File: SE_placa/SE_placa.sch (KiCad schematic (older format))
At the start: 53 parts, among them J1 5V, J2 Micro_SD_Card_Det_Hirose_DM3AT, J3 Conn_02x07_ESP32_IO, J4 I2C-0, J5 I2C-1, J6 Conn_02x03_LORA_IO, J7 U.FL-R-SMT(01), J8 UART, J9 Connector Bateria, Q1 BSS138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

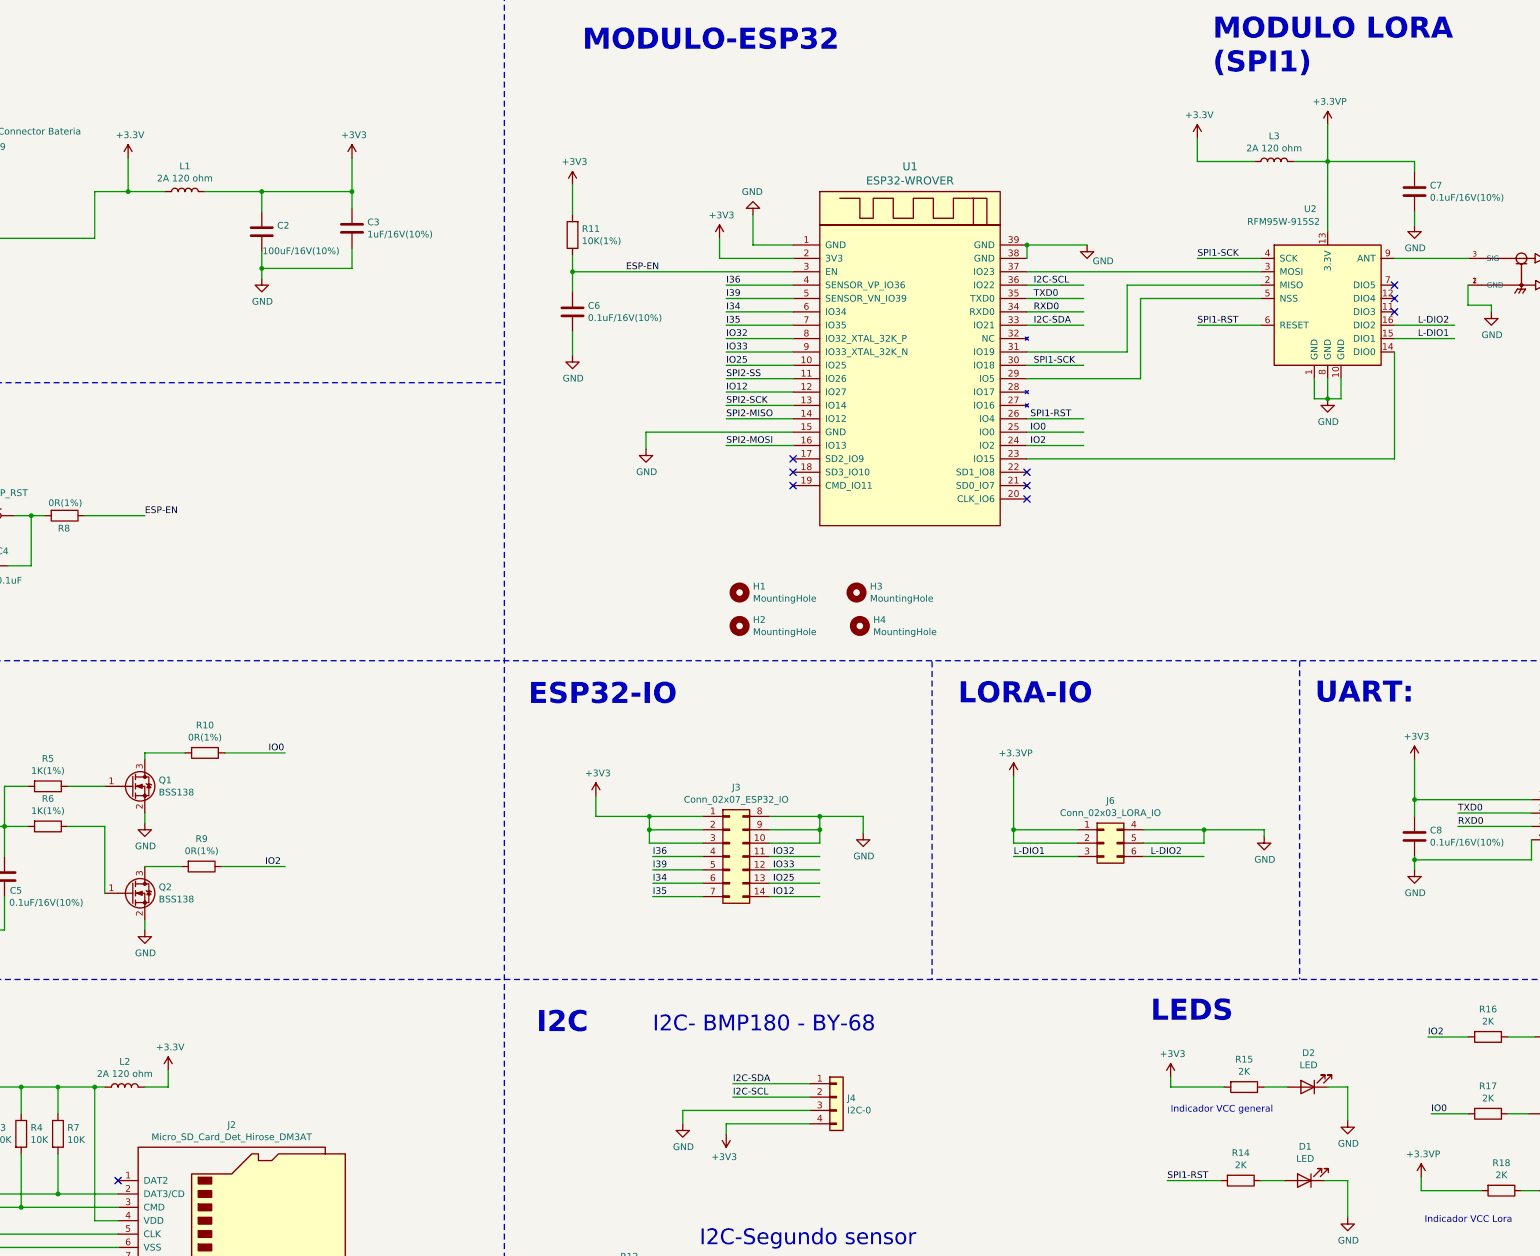
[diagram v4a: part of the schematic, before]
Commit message: Ruteo 2
Aumento el ancho de las pistas de señales a 0.4 m
aumento las pistas de alimentacion a 1 mm
modifico ubicacion de elementos para mejorar ruteo evitando pasar por debajo de elementos
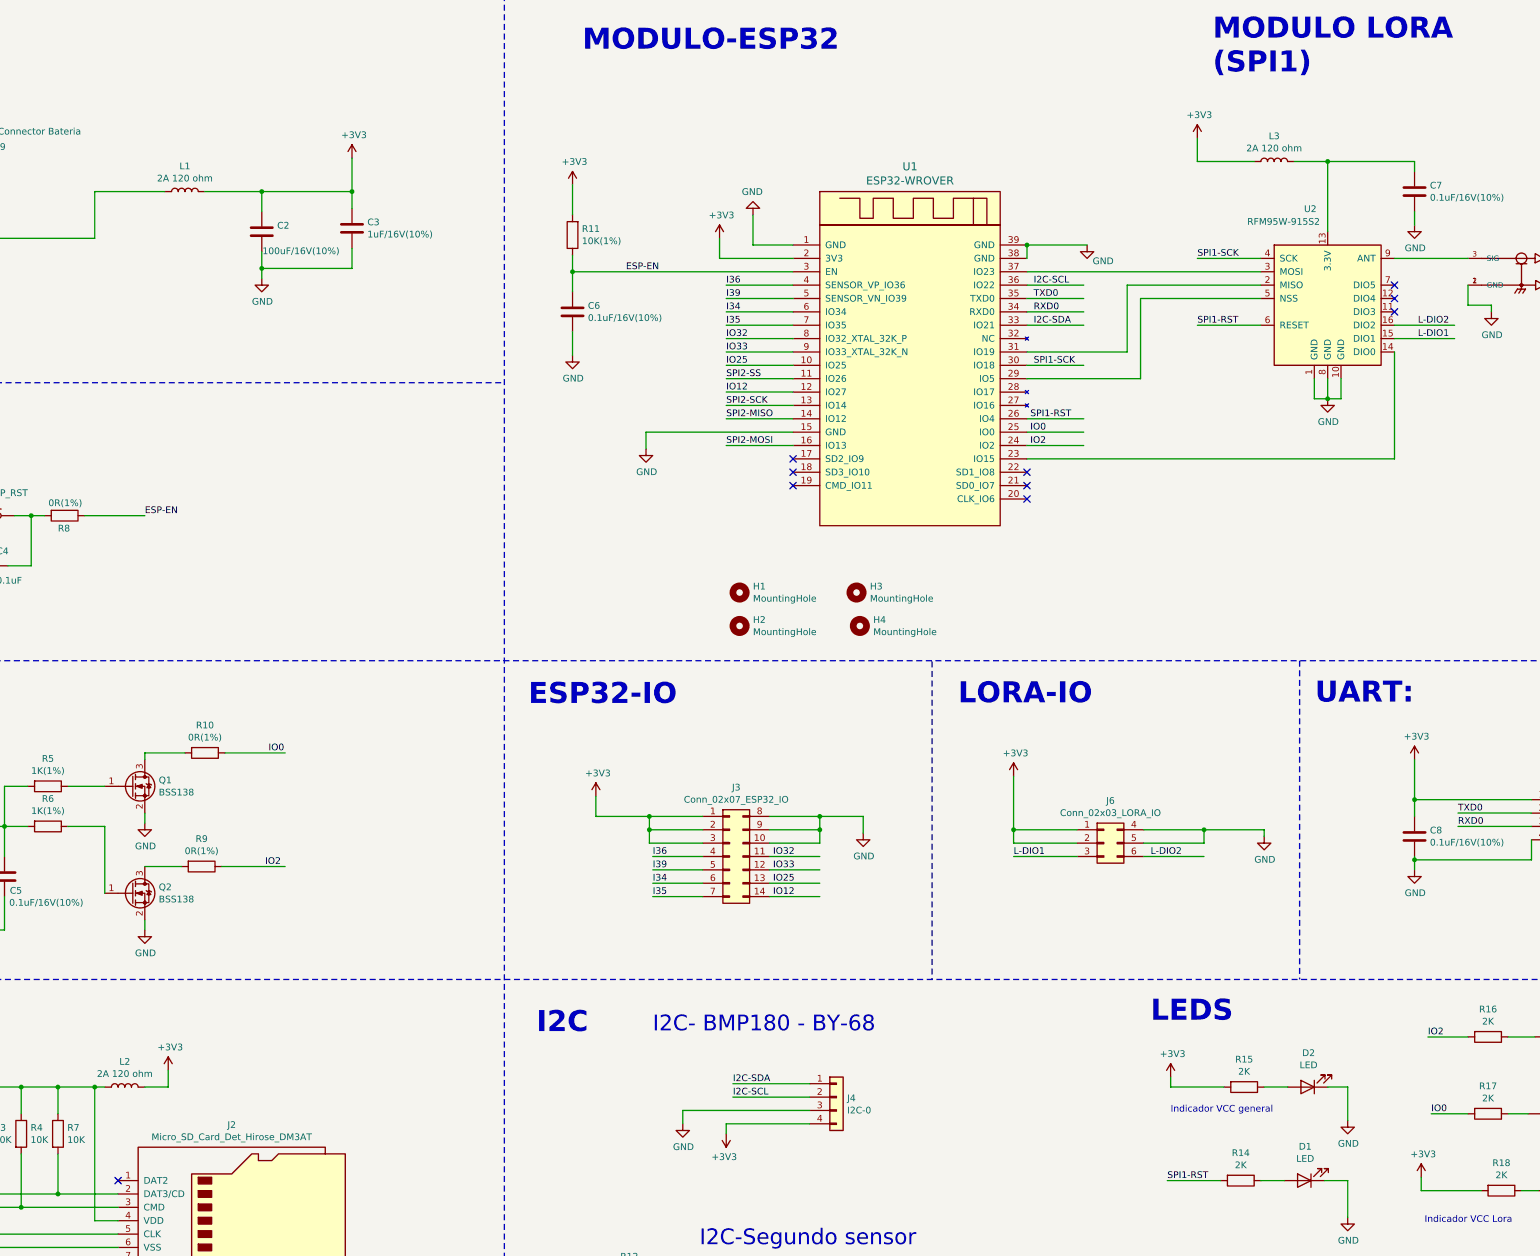
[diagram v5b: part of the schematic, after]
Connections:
- net labels removed: +3.3V, +3.3VP
- wire segments 228 -> 225
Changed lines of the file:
@@
-$EndComp
-$Comp
-L power:+3.3V #PWR027
-U 1 1 607CBBE1
-P 12325 1600
-F 0 "#PWR027" H 12325 1450 50  0001 C CNN
-F 1 "+3.3V" H 12340 1773 50  0000 C CNN
-F 2 "" H 12325 1600 50  0001 C CNN
-F 3 "" H 12325 1600 50  0001 C CNN
-	1    12325 1600
-	1    0    0    -1
 $EndComp
 $Comp
@@
 	4625 8575 4625 8700
 $Comp
-L power:+3.3V #PWR011
-U 1 1 6089EF62
-P 4625 8575
-F 0 "#PWR011" H 4625 8425 50  0001 C CNN
-F 1 "+3.3V" H 4640 8748 50  0000 C CNN
-F 2 "" H 4625 8575 50  0001 C CNN
-F 3 "" H 4625 8575 50  0001 C CNN
-	1    4625 8575
-	1    0    0    -1
-$EndComp
-$Comp
 L Device:L L2
 U 1 1 60AE3C36
@@
 Wire Wire Line
 	11925 6975 12375 6975
-$Comp
-L power:+3.3VP #PWR024
-U 1 1 61D4E127
-P 10950 6375
-F 0 "#PWR024" H 11100 6325 50  0001 C CNN
-F 1 "+3.3VP" H 10965 6548 50  0000 C CNN
-F 2 "" H 10950 6375 50  0001 C CNN
-F 3 "" H 10950 6375 50  0001 C CNN
-	1    10950 6375
-	1    0    0    -1
-$EndComp
 Wire Wire Line
 	10950 6375 10950 6775
-$Comp
-L power:+3.3VP #PWR029
-U 1 1 61D757B6
-P 13300 1500
-F 0 "#PWR029" H 13450 1450 50  0001 C CNN
-F 1 "+3.3VP" H 13315 1673 50  0000 C CNN
-F 2 "" H 13300 1500 50  0001 C CNN
-F 3 "" H 13300 1500 50  0001 C CNN
-	1    13300 1500
-	1    0    0    -1
-$EndComp
-Wire Wire Line
-	13300 1500 13300 1775
 Wire Wire Line
 	13950 6975 13950 7000
@@
 Wire Wire Line
 	13450 9400 13450 9675
-$Comp
-L power:+3.3VP #PWR036
-U 1 1 620B9942
-P 14000 9375
-F 0 "#PWR036" H 14150 9325 50  0001 C CNN
-F 1 "+3.3VP" H 14015 9548 50  0000 C CNN
-F 2 "" H 14000 9375 50  0001 C CNN
-F 3 "" H 14000 9375 50  0001 C CNN
-	1    14000 9375
-	1    0    0    -1
-$EndComp
 Wire Wire Line
 	14000 9375 14000 9475
@@
 F 3 "~" H 5325 2300 50  0001 C CNN
 	1    5325 2300
-	1    0    0    -1
-$EndComp
-$Comp
-L power:+3.3V #PWR041
-U 1 1 60B718CF
-P 4325 1750
-AR Path="/60B718CF" Ref="#PWR041"  Part="1"
-AR Path="/609FB393/60B718CF" Ref="#PWR?"  Part="1"
-F 0 "#PWR041" H 4325 1600 50  0001 C CNN
-F 1 "+3.3V" H 4340 1923 50  0000 C CNN
-F 2 "" H 4325 1750 50  0001 C CNN
-F 3 "" H 4325 1750 50  0001 C CNN
-	1    4325 1750
 	1    0    0    -1
 $EndComp
@@
 Connection ~ 5325 2000
 Wire Wire Line
-	4600 2000 4325 2000
-Wire Wire Line
-	4325 1750 4325 2000
-Connection ~ 4325 2000
-Wire Wire Line
-	4325 2000 4075 2000
+	4075 2000 4600 2000
+$Comp
+L power:+3V3 #PWR0103
+U 1 1 60F618C6
+P 12325 1600
+F 0 "#PWR0103" H 12325 1450 50  0001 C CNN
+F 1 "+3V3" H 12340 1773 50  0000 C CNN
+F 2 "" H 12325 1600 50  0001 C CNN
+F 3 "" H 12325 1600 50  0001 C CNN
+	1    12325 1600
+	1    0    0    -1
+$EndComp
+$Comp
+L power:+3V3 #PWR0104
+U 1 1 60FBAEA9
+P 10950 6375
+F 0 "#PWR0104" H 10950 6225 50  0001 C CNN
+F 1 "+3V3" H 10965 6548 50  0000 C CNN
+F 2 "" H 10950 6375 50  0001 C CNN
+F 3 "" H 10950 6375 50  0001 C CNN
+	1    10950 6375
+	1    0    0    -1
+$EndComp
+$Comp
+L power:+3V3 #PWR0105
+U 1 1 60FC1BE6
+P 4625 8575
+F 0 "#PWR0105" H 4625 8425 50  0001 C CNN
+F 1 "+3V3" H 4640 8748 50  0000 C CNN
+F 2 "" H 4625 8575 50  0001 C CNN
+F 3 "" H 4625 8575 50  0001 C CNN
+	1    4625 8575
+	1    0    0    -1
+$EndComp
+$Comp
+L power:+3V3 #PWR?
+U 1 1 61008AFD
+P 14000 9375
+F 0 "#PWR?" H 14000 9225 50  0001 C CNN
+F 1 "+3V3" H 14015 9548 50  0000 C CNN
+F 2 "" H 14000 9375 50  0001 C CNN
+F 3 "" H 14000 9375 50  0001 C CNN
+	1    14000 9375
+	1    0    0    -1
+$EndComp
 $EndSCHEMATC

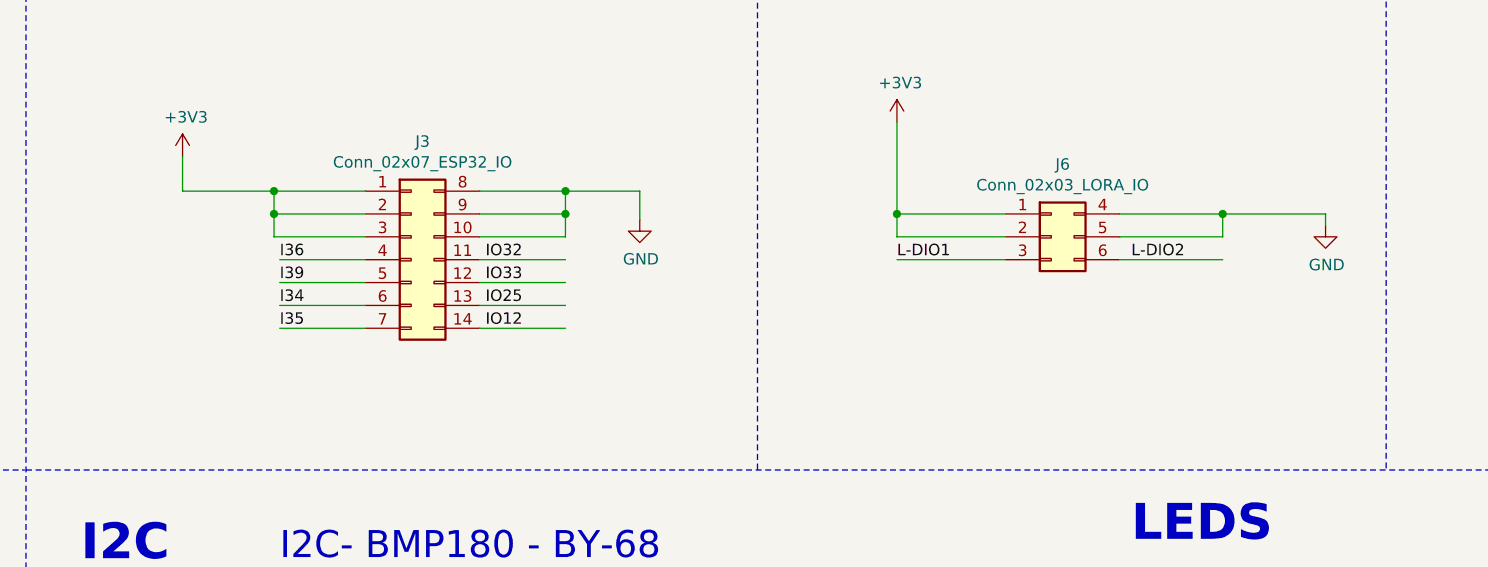
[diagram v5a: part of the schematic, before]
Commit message: Ruteo 3
1. Cambio orden de los pines de I/O para hacer mas facil el ruteo de los conectores, modifico ubicacion de I/Os del Lora
2. Cambio huella del LTC 3441 al parecer la que tenia creaba conflictos con las rutas y sus anchos
3. cambio el esquema de Net classes a default, arreglando el tamaño de las rutas y de las vias .
4. Modifico la ruta a 0.3 mm , agrego esto a pre definidas
5. agrego ruta de 1 mm y vias de 1.8 mm para alimentaciones
6. cambio ubicaciones de conectorres de bateria y de panel solar
7. cambio ubicacion del TP4056 y modifico la ubicacion de los componentes cercanos.
8. Falta agregar plano de tierra en las dos caras y modificar salida de potencia de la entrada y la salida del LTC 3441
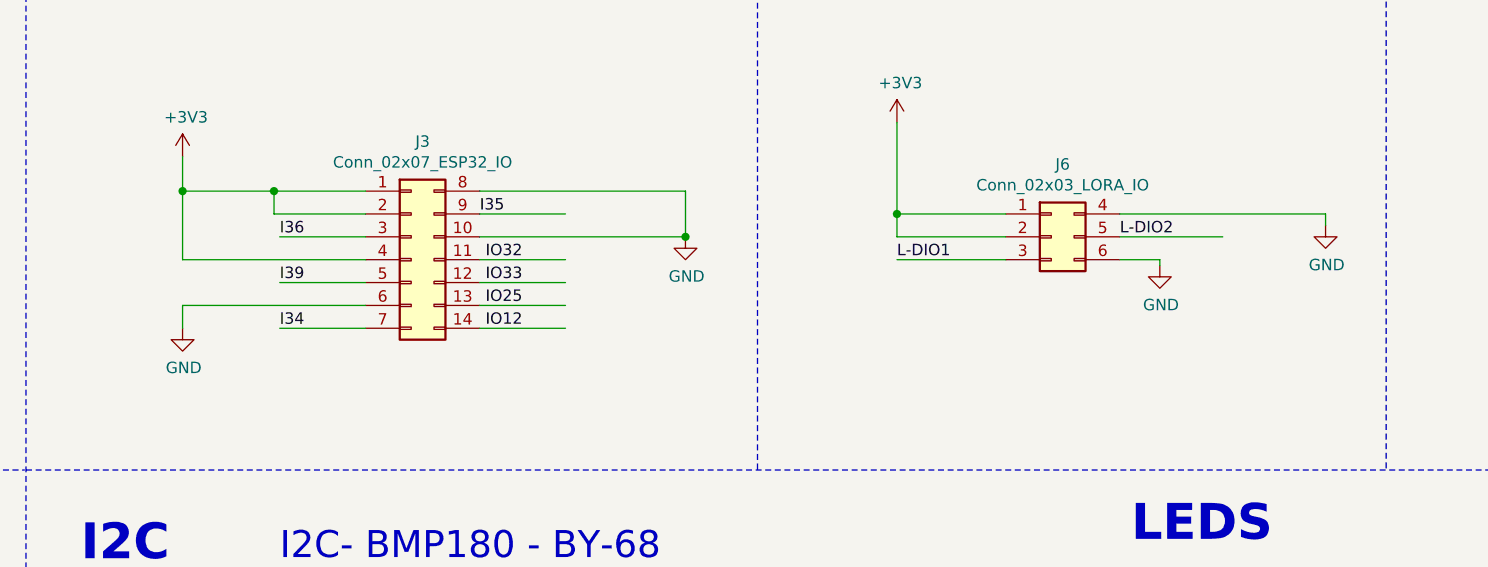
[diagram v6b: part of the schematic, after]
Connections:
- wire segments 225 -> 222
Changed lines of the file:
@@
 Text Notes 11975 8225 0    157  ~ 31
 LEDS
-Text Label 8250 6975 0    50   ~ 0
+Text Label 8250 6875 0    50   ~ 0
 I36
 Text Label 8250 7075 0    50   ~ 0
 I39
-Text Label 8250 7175 0    50   ~ 0
+Text Label 8250 7275 0    50   ~ 0
 I34
-Text Label 8250 7275 0    50   ~ 0
-I35
 $Comp
 L power:GND #PWR018
@@
 Text Label 13975 3000 0    50   ~ 0
 L-DIO2
-Text Label 11975 6975 0    50   ~ 0
+Text Label 11925 6875 0    50   ~ 0
 L-DIO2
 Text Label 10950 6975 0    50   ~ 0
@@
 	8225 6675 8625 6675
 Wire Wire Line
-	8625 6875 8225 6875
-Wire Wire Line
-	8225 6875 8225 6775
-Connection ~ 8225 6775
-Wire Wire Line
-	9125 6675 9500 6675
-Wire Wire Line
-	9825 6675 9825 6800
-Wire Wire Line
-	9125 6775 9500 6775
-Wire Wire Line
-	9500 6775 9500 6675
-Connection ~ 9500 6675
-Wire Wire Line
-	9500 6675 9825 6675
-Wire Wire Line
-	9125 6875 9500 6875
-Wire Wire Line
-	9500 6875 9500 6775
-Connection ~ 9500 6775
-Wire Wire Line
 	9125 6975 9500 6975
 Wire Wire Line
@@
 	9125 7275 9500 7275
 Wire Wire Line
-	8250 6975 8625 6975
+	8250 6875 8625 6875
 Wire Wire Line
 	8250 7075 8625 7075
-Wire Wire Line
-	8250 7175 8625 7175
 Wire Wire Line
 	8250 7275 8625 7275
@@
 $EndComp
 Wire Wire Line
-	11925 6775 12375 6775
-Wire Wire Line
 	12825 6775 12825 6825
 Wire Wire Line
 	11925 6875 12375 6875
-Wire Wire Line
-	12375 6875 12375 6775
-Connection ~ 12375 6775
-Wire Wire Line
-	12375 6775 12825 6775
-Wire Wire Line
-	11925 6975 12375 6975
 Wire Wire Line
 	10950 6375 10950 6775
@@
 L power:GND #PWR0102
 U 1 1 60FEDC40
-P 9825 6800
-F 0 "#PWR0102" H 9825 6550 50  0001 C CNN
-F 1 "GND" H 9830 6627 50  0000 C CNN
-F 2 "" H 9825 6800 50  0001 C CNN
-F 3 "" H 9825 6800 50  0001 C CNN
-	1    9825 6800
+P 10025 6875
+F 0 "#PWR0102" H 10025 6625 50  0001 C CNN
+F 1 "GND" H 10030 6702 50  0000 C CNN
+F 2 "" H 10025 6875 50  0001 C CNN
+F 3 "" H 10025 6875 50  0001 C CNN
+	1    10025 6875
 	1    0    0    -1
 $EndComp
@@
 $EndComp
 $Comp
-L power:+3V3 #PWR?
+L power:+3V3 #PWR0106
 U 1 1 61008AFD
 P 14000 9375
-F 0 "#PWR?" H 14000 9225 50  0001 C CNN
+F 0 "#PWR0106" H 14000 9225 50  0001 C CNN
 F 1 "+3V3" H 14015 9548 50  0000 C CNN
 F 2 "" H 14000 9375 50  0001 C CNN
@@
 	1    0    0    -1
 $EndComp
+Wire Wire Line
+	11925 6775 12825 6775
+$Comp
+L power:GND #PWR?
+U 1 1 610D8D32
+P 12100 7000
+F 0 "#PWR?" H 12100 6750 50  0001 C CNN
+F 1 "GND" H 12105 6827 50  0000 C CNN
+F 2 "" H 12100 7000 50  0001 C CNN
+F 3 "" H 12100 7000 50  0001 C CNN
+	1    12100 7000
+	1    0    0    -1
+$EndComp
+Wire Wire Line
+	11925 6975 12100 6975
+Wire Wire Line
+	12100 6975 12100 7000
+Wire Wire Line
+	9125 6775 9500 6775
+Text Label 9125 6775 0    50   ~ 0
+I35
+Wire Wire Line
+	10025 6875 9125 6875
+Wire Wire Line
+	10025 6875 10025 6675
+Connection ~ 10025 6875
+Wire Wire Line
+	9125 6675 10025 6675
+Wire Wire Line
+	8625 6975 7825 6975
+Wire Wire Line
+	7825 6975 7825 6675
+Connection ~ 7825 6675
+Wire Wire Line
+	8625 7175 7825 7175
+Wire Wire Line
+	7825 7175 7825 7275
+$Comp
+L power:GND #PWR?
+U 1 1 611AF203
+P 7825 7275
+F 0 "#PWR?" H 7825 7025 50  0001 C CNN
+F 1 "GND" H 7830 7102 50  0000 C CNN
+F 2 "" H 7825 7275 50  0001 C CNN
+F 3 "" H 7825 7275 50  0001 C CNN
+	1    7825 7275
+	1    0    0    -1
+$EndComp
